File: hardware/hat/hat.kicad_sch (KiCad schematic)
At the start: 16 parts, among them J101 GPIO, J102 Uart, U101 CAT24C256, U102 TPS7A20xxxDBV, U103 Oled

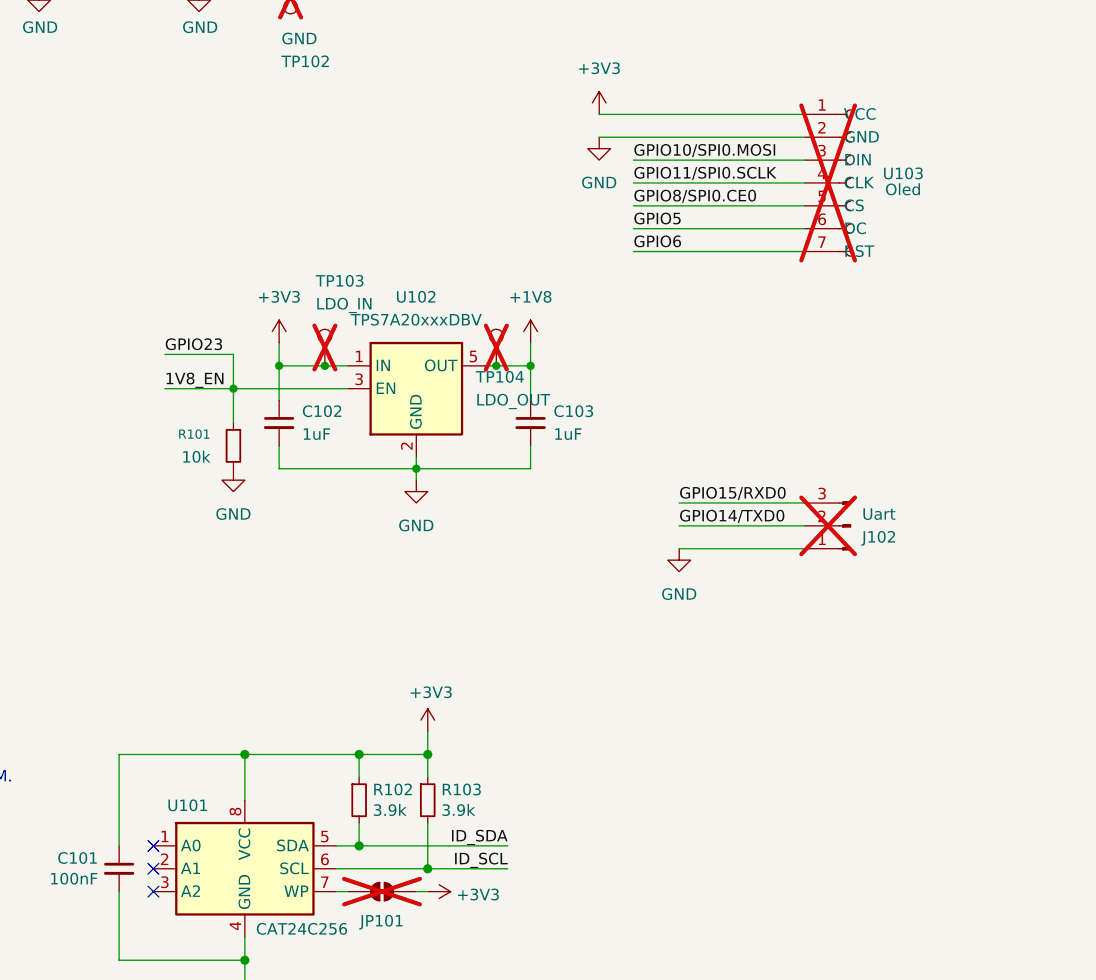
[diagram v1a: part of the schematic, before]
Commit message: move ldo into audio sheet
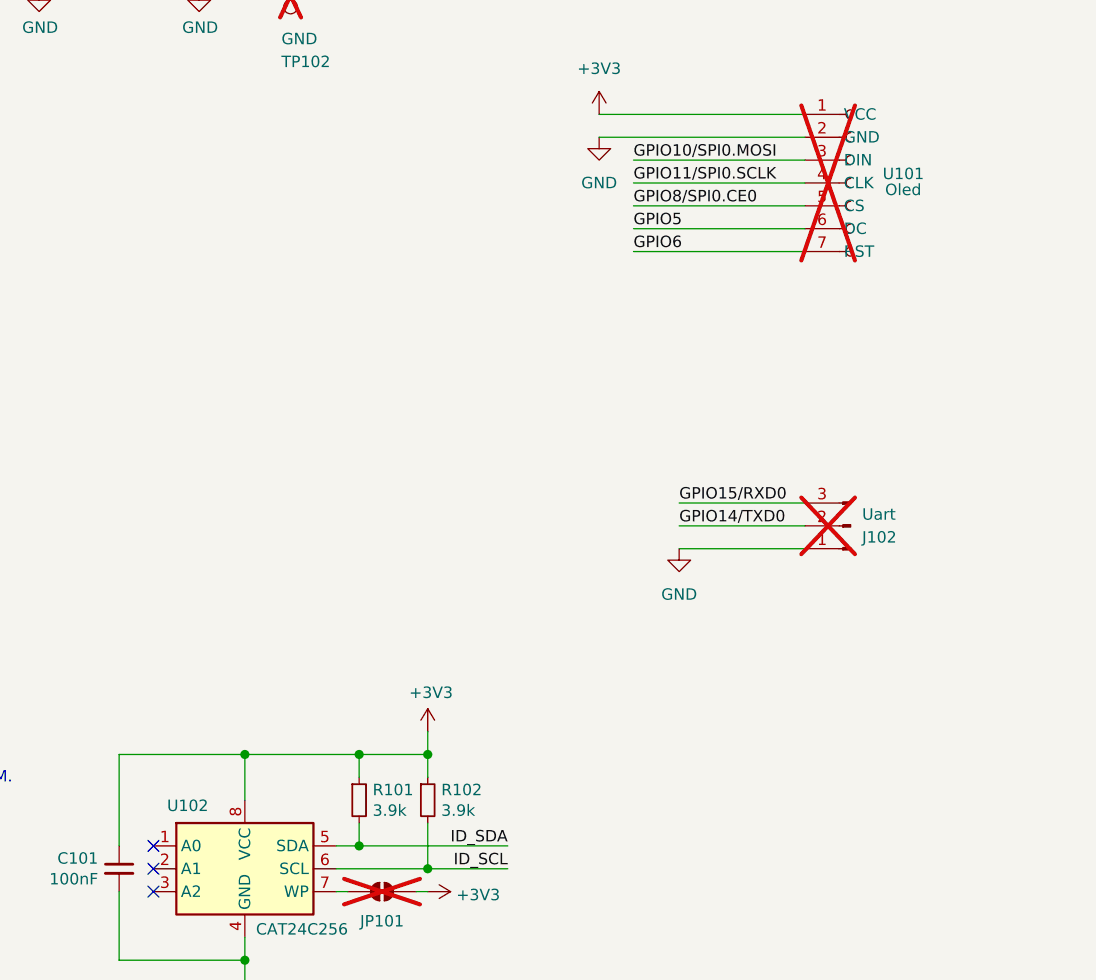
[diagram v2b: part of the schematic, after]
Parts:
- removed C102, C103: 1uF, Capacitor_SMD:C_0805_2012Metric, symbol Device:C_Small
- removed R101: 10k, Resistor_SMD:R_0805_2012Metric, symbol Device:R_Small
- removed TP103: LDO_IN, TestPoint:TestPoint_Pad_D2.0mm, symbol Connector:TestPoint
- removed TP104: LDO_OUT, TestPoint:TestPoint_Pad_D2.0mm, symbol Connector:TestPoint
- removed U102: TPS7A20xxxDBV, Package_TO_SOT_SMD:SOT-23-5, symbol Regulator_Linear:TPS7A20xxxDBV
- renumbered R102 to R101, R103 to R102, U103 to U101, U101 to U102
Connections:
- net 1V8_EN renamed GPIO23

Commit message: use H label for 1v8en
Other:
- sheet codec ports: added CODEC_1V8EN; removed none
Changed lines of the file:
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@@
+	(wire
+		(pts
+			(xy 137.16 69.85) (xy 151.13 69.85)
+		)
+		(stroke
+			(width 0)
+			(type default)
+		)
+	)
 	(wire
 		(pts
@@
 			)
 			(justify right bottom)
+		)
+	)
+	(label "GPIO23"
+		(at 137.16 69.85 0)
+		(effects
+			(font
+				(size 1.27 1.27)
+			)
+			(justify left bottom)
 		)
 	)
@@
 			(effects
 				(font
+					(size 1.27 1.27)
+				)
+				(justify left)
+			)
+		)
+		(pin "CODEC_1V8EN" input
+			(at 151.13 69.85 180)
+			(effects
+				(font
